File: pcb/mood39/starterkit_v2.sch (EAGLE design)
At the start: 7 parts, among them IC1 TINY85

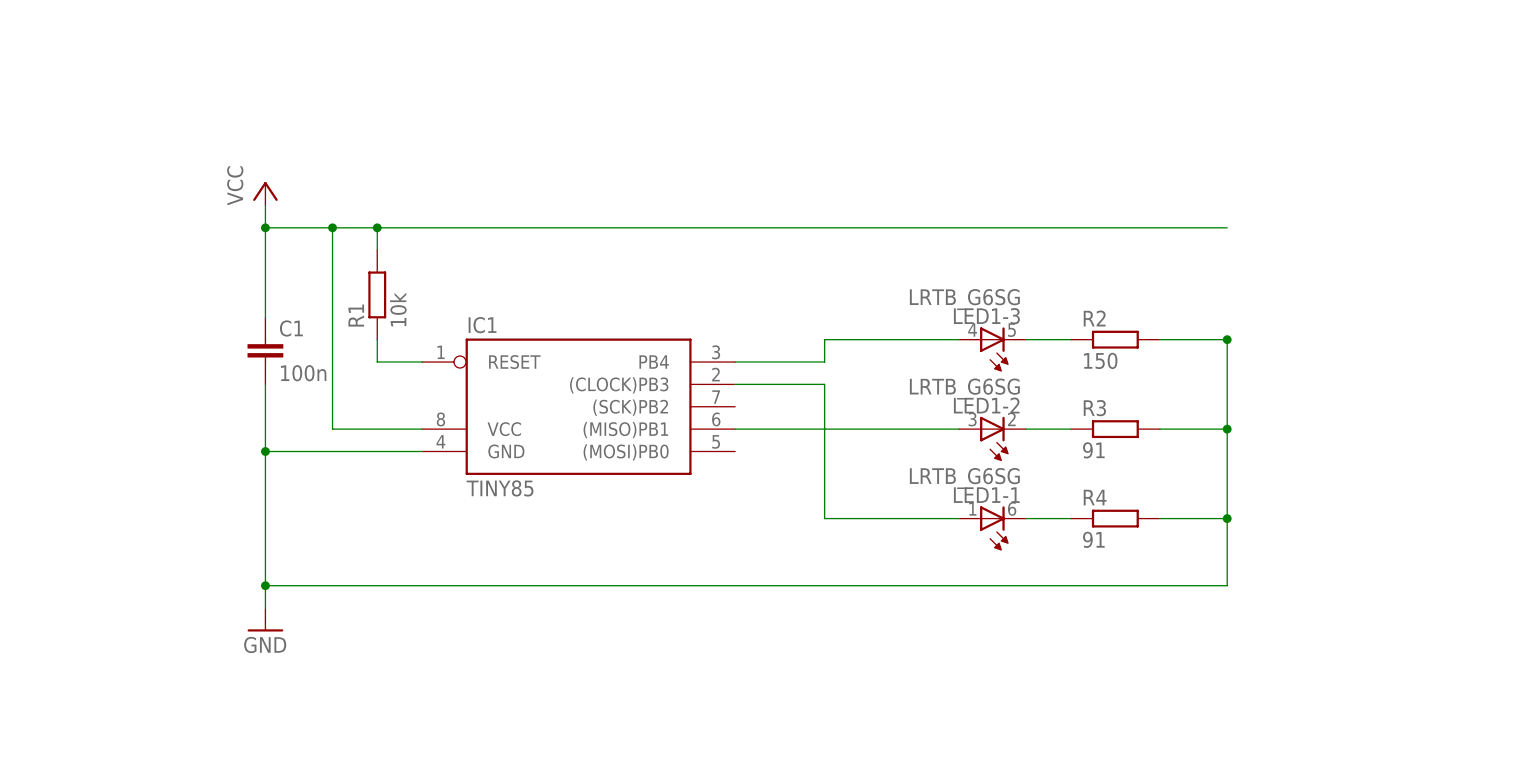
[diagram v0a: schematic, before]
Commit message: add some connectors and the voltage regulator
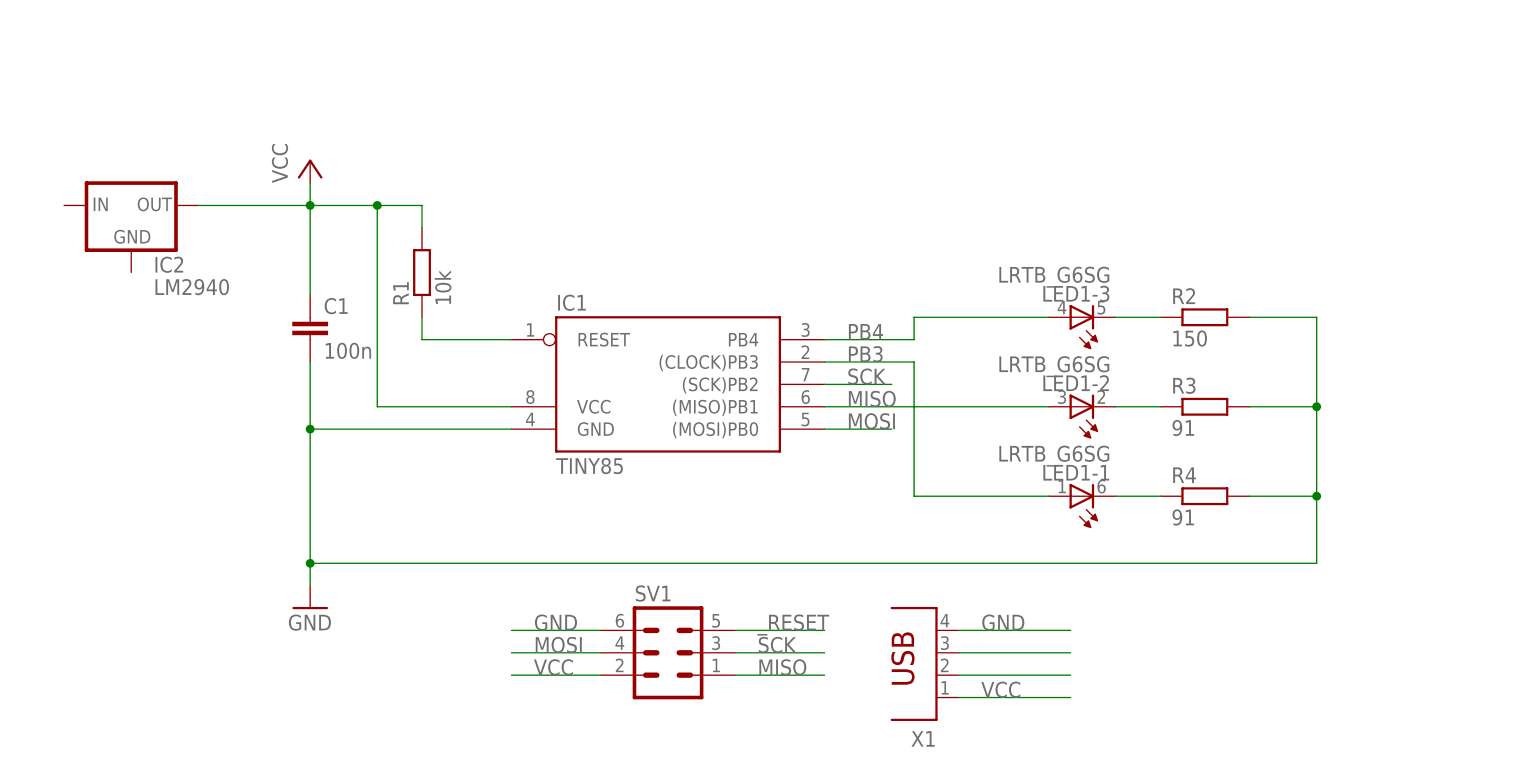
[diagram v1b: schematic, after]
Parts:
- added IC2: LM2940, v-reg:78XXL
- added SV1: (no value), con-ml:ML6
- added X1: (no value), con-berg:PN61729
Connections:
- net N$1 renamed PB4
- net N$3 renamed PB3
- removed net N$2: IC1.(MISO)PB1, LED1-2.A
- removed net N$4: IC1.RESET, R1.1
- new net MISO: IC1.(MISO)PB1, LED1-2.A, SV1.1
- new net MOSI: IC1.(MOSI)PB0, SV1.4
- new net SCK: IC1.(SCK)PB2, SV1.3
- new net USBD+: X1.3
- new net USBD-: X1.2
- new net _RESET: IC1.RESET, R1.1, SV1.5
- net GND: now also SV1.6, X1.4
- net VCC: now also IC2.OUT, SV1.2, X1.1
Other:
- moved on the sheet: C1, IC1, LED1-1, LED1-2, LED1-3, R1, R2, R3, R4

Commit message: add board (not routed) and design rules
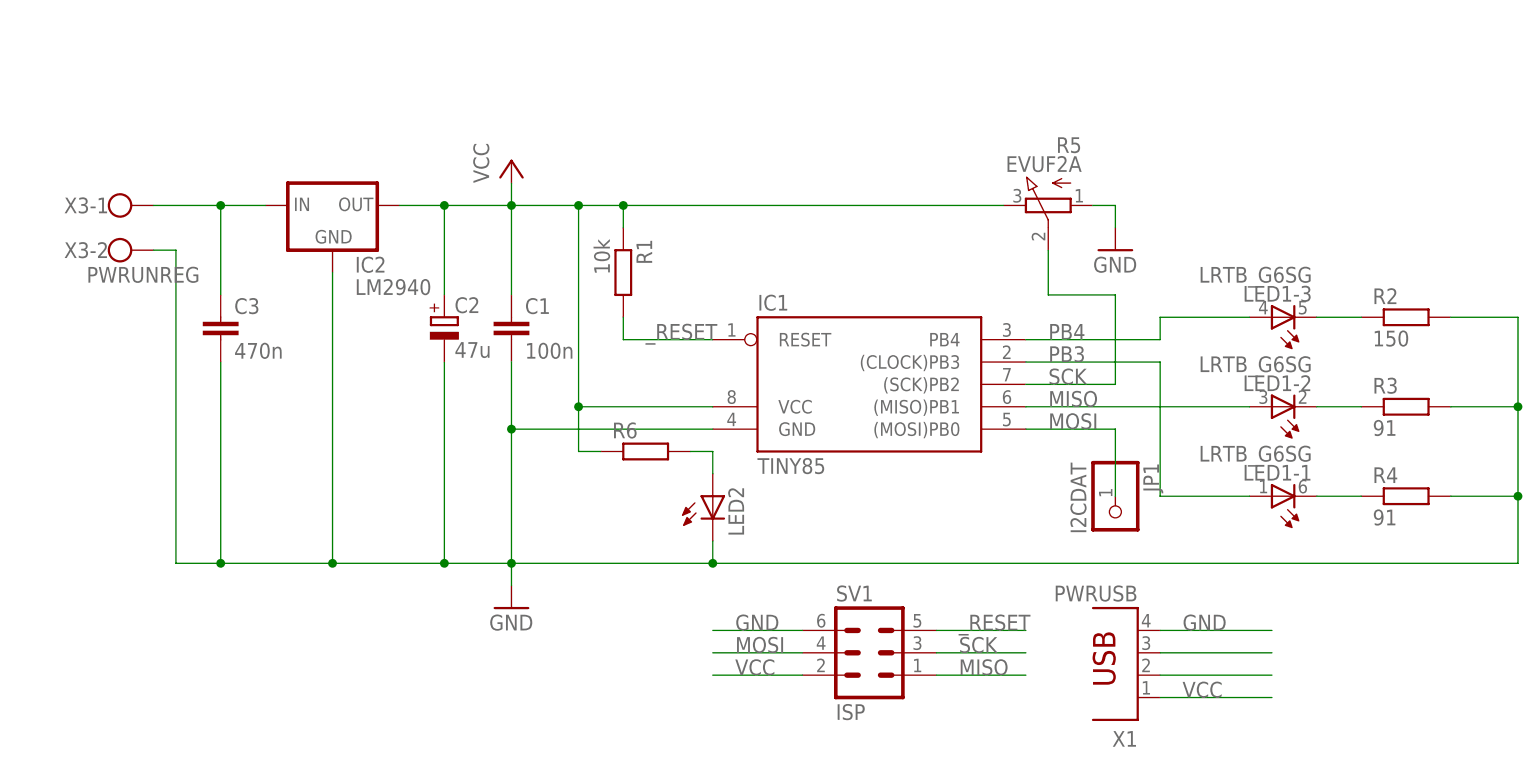
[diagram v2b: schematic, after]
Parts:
- added C2: 47u, rcl:CPOL-EUE2.5-5
- added C3: 470n, rcl:C-EU025-025X050
- added JP1: I2CDAT, pinhead:PINHD-1X1
- added LED2: (no value), led:LED3MM
- added R5: EVUF2A, pot:EVUF2A
- added R6: (no value), rcl:R-EU_R0805
- added X3: PWRUNREG, con-wago-500:W237-102
- C1: device rcl:C-EU025-025X050 -> rcl:C-EUC0805
- IC2: device v-reg:78XXL -> v-reg:78XXS
- R1, R2, R3, R4: device rcl:R-EU_0204/7 -> rcl:R-EU_R0805
- SV1: value (none) -> ISP
- X1: value (none) -> PWRUSB
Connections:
- new net N$1: LED2.A, R6.2
- new net N$2: C3.1, IC2.IN, X3-1.KL
- net GND: now also C2.-, C3.2, IC2.GND, LED2.C, R5.A, X3-2.KL
- net MOSI: now also JP1.1
- net SCK: now also R5.S
- net VCC: now also C2.+, R1.1, R5.E, R6.1; no longer R1.2
- net _RESET: now also R1.2; no longer R1.1
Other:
- moved on the sheet: C1, IC1, LED1-1, LED1-2, LED1-3, R1, R2, R3, R4, SV1, X1

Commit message: start routing
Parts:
- C3: device rcl:C-EU025-025X050 -> rcl:C-EUC0805
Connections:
- net N$2 renamed V+
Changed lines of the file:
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@@
 <clearance class="0" value="0.355"/>
+</class>
+<class number="1" name="supply" width="0.4064" drill="0">
 </class>
 </classes>
@@
 <part name="X3" library="con-wago-500" deviceset="W237-102" device="" value="PWRUNREG"/>
 <part name="C2" library="rcl" deviceset="CPOL-EU" device="E2.5-5" value="47u"/>
-<part name="C3" library="rcl" deviceset="C-EU" device="025-025X050" value="470n"/>
+<part name="C3" library="rcl" deviceset="C-EU" device="C0805" value="470n"/>
 <part name="R5" library="pot" deviceset="EVU" device="A" technology="F2"/>
 <part name="JP1" library="pinhead" deviceset="PINHD-1X1" device="" value="I2CDAT"/>
@@
 </segment>
 </net>
-<net name="GND" class="0">
+<net name="GND" class="1">
 <segment>
 <pinref part="C1" gate="G$1" pin="2"/>
@@
 </segment>
 </net>
-<net name="VCC" class="0">
+<net name="VCC" class="1">
 <segment>
 <pinref part="IC1" gate="G$1" pin="VCC"/>
@@
 </segment>
 </net>
-<net name="N$2" class="0">
+<net name="V+" class="1">
 <segment>
 <pinref part="X3" gate="-1" pin="KL"/>
@@
 <wire x1="-10.16" y1="68.58" x2="-10.16" y2="78.74" width="0.1524" layer="91"/>
 <junction x="-10.16" y="78.74"/>
-</segment>
-</net>
+<label x="-15.24" y="78.74" size="1.778" layer="95"/>
+</segment>
+</net>

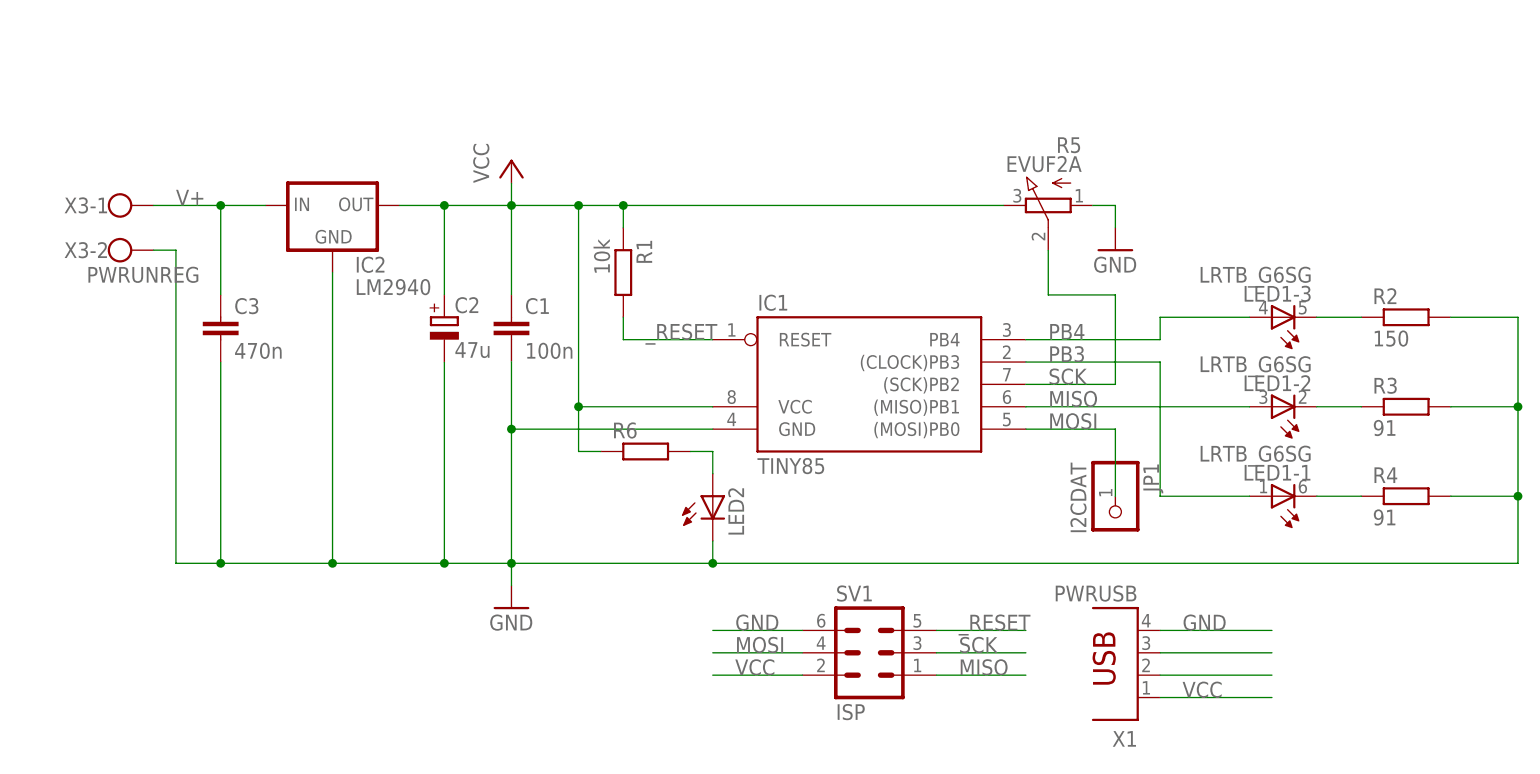
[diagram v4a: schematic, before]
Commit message: routing to a point where the right packages are needed
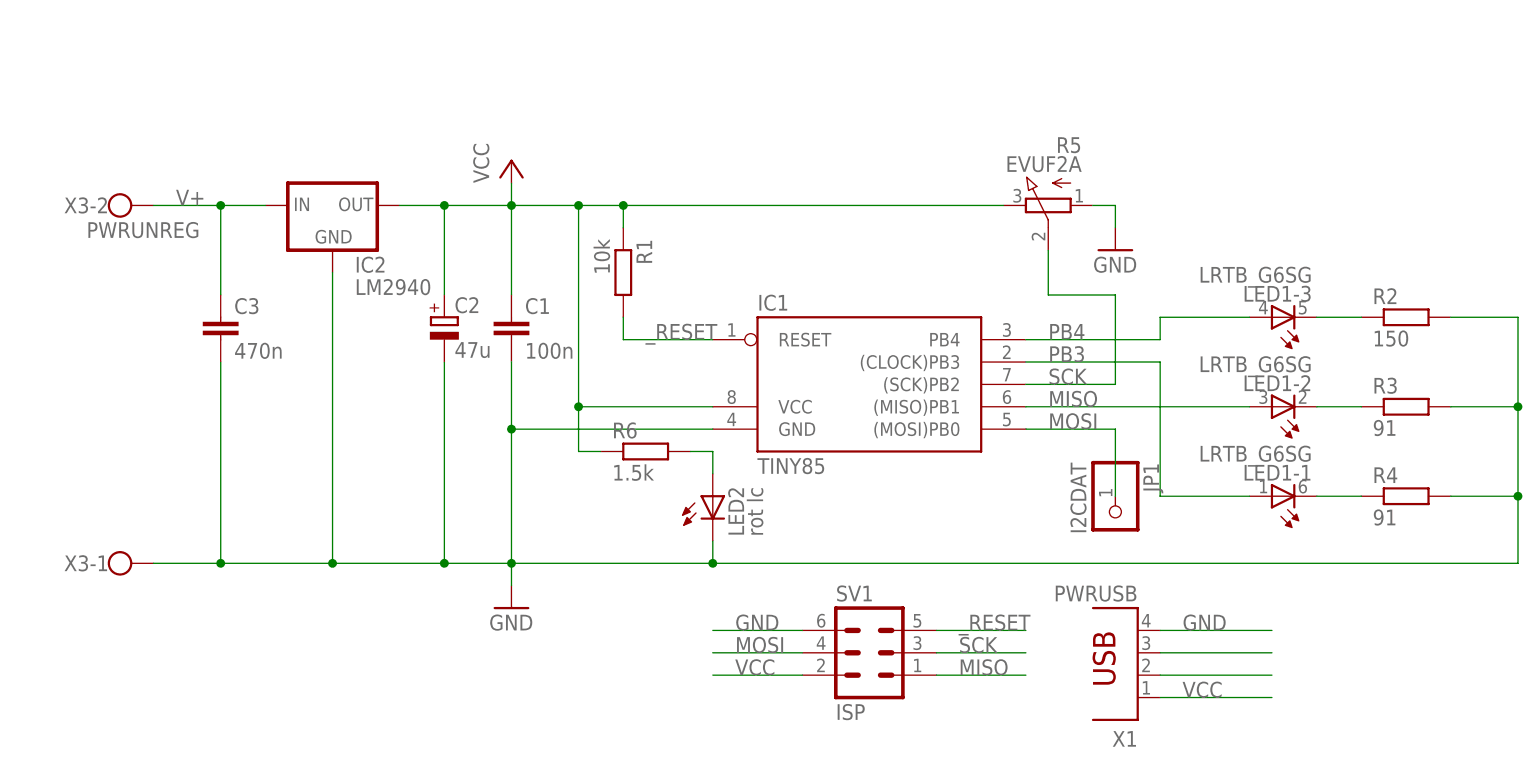
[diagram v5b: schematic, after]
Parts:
- LED2: value (none) -> rot lc
- R6: value (none) -> 1.5k
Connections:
- net GND: now also X3-1.KL; no longer X3-2.KL
- net V+: now also X3-2.KL; no longer X3-1.KL
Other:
- moved on the sheet: X3-1, X3-2
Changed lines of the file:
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@@
 <grid distance="0.1" unitdist="inch" unit="inch" style="lines" multiple="1" display="no" altdistance="0.01" altunitdist="inch" altunit="inch"/>
 <layers>
-<layer number="1" name="Top" color="4" fill="1" visible="yes" active="no"/>
-<layer number="16" name="Bottom" color="1" fill="1" visible="yes" active="no"/>
-<layer number="17" name="Pads" color="2" fill="1" visible="yes" active="no"/>
-<layer number="18" name="Vias" color="2" fill="1" visible="yes" active="no"/>
-<layer number="19" name="Unrouted" color="6" fill="1" visible="yes" active="no"/>
-<layer number="20" name="Dimension" color="15" fill="1" visible="yes" active="no"/>
-<layer number="21" name="tPlace" color="7" fill="1" visible="yes" active="no"/>
-<layer number="22" name="bPlace" color="7" fill="1" visible="yes" active="no"/>
-<layer number="23" name="tOrigins" color="15" fill="1" visible="yes" active="no"/>
-<layer number="24" name="bOrigins" color="15" fill="1" visible="yes" active="no"/>
-<layer number="25" name="tNames" color="7" fill="1" visible="yes" active="no"/>
-<layer number="26" name="bNames" color="7" fill="1" visible="yes" active="no"/>
-<layer number="27" name="tValues" color="7" fill="1" visible="yes" active="no"/>
-<layer number="28" name="bValues" color="7" fill="1" visible="yes" active="no"/>
+<layer number="1" name="Top" color="4" fill="1" visible="no" active="no"/>
+<layer number="16" name="Bottom" color="1" fill="1" visible="no" active="no"/>
+<layer number="17" name="Pads" color="2" fill="1" visible="no" active="no"/>
+<layer number="18" name="Vias" color="2" fill="1" visible="no" active="no"/>
+<layer number="19" name="Unrouted" color="6" fill="1" visible="no" active="no"/>
+<layer number="20" name="Dimension" color="15" fill="1" visible="no" active="no"/>
+<layer number="21" name="tPlace" color="7" fill="1" visible="no" active="no"/>
+<layer number="22" name="bPlace" color="7" fill="1" visible="no" active="no"/>
+<layer number="23" name="tOrigins" color="15" fill="1" visible="no" active="no"/>
+<layer number="24" name="bOrigins" color="15" fill="1" visible="no" active="no"/>
+<layer number="25" name="tNames" color="7" fill="1" visible="no" active="no"/>
+<layer number="26" name="bNames" color="7" fill="1" visible="no" active="no"/>
+<layer number="27" name="tValues" color="7" fill="1" visible="no" active="no"/>
+<layer number="28" name="bValues" color="7" fill="1" visible="no" active="no"/>
 <layer number="29" name="tStop" color="7" fill="3" visible="no" active="no"/>
 <layer number="30" name="bStop" color="7" fill="6" visible="no" active="no"/>
@@
 <layer number="35" name="tGlue" color="7" fill="4" visible="no" active="no"/>
 <layer number="36" name="bGlue" color="7" fill="5" visible="no" active="no"/>
-<layer number="37" name="tTest" color="7" fill="1" visible="yes" active="no"/>
-<layer number="38" name="bTest" color="7" fill="1" visible="yes" active="no"/>
+<layer number="37" name="tTest" color="7" fill="1" visible="no" active="no"/>
+<layer number="38" name="bTest" color="7" fill="1" visible="no" active="no"/>
 <layer number="39" name="tKeepout" color="4" fill="11" visible="no" active="no"/>
 <layer number="40" name="bKeepout" color="1" fill="11" visible="no" active="no"/>
@@
 <layer number="44" name="Drills" color="7" fill="1" visible="no" active="no"/>
 <layer number="45" name="Holes" color="7" fill="1" visible="no" active="no"/>
-<layer number="46" name="Milling" color="3" fill="1" visible="yes" active="no"/>
-<layer number="47" name="Measures" color="7" fill="1" visible="yes" active="no"/>
-<layer number="48" name="Document" color="7" fill="1" visible="yes" active="no"/>
-<layer number="49" name="Reference" color="7" fill="1" visible="yes" active="no"/>
-<layer number="51" name="tDocu" color="7" fill="1" visible="yes" active="no"/>
-<layer number="52" name="bDocu" color="7" fill="1" visible="yes" active="no"/>
+<layer number="46" name="Milling" color="3" fill="1" visible="no" active="no"/>
+<layer number="47" name="Measures" color="7" fill="1" visible="no" active="no"/>
+<layer number="48" name="Document" color="7" fill="1" visible="no" active="no"/>
+<layer number="49" name="Reference" color="7" fill="1" visible="no" active="no"/>
+<layer number="51" name="tDocu" color="7" fill="1" visible="no" active="no"/>
+<layer number="52" name="bDocu" color="7" fill="1" visible="no" active="no"/>
 <layer number="91" name="Nets" color="2" fill="1" visible="yes" active="yes"/>
 <layer number="92" name="Busses" color="1" fill="1" visible="yes" active="yes"/>
@@
 <part name="JP1" library="pinhead" deviceset="PINHD-1X1" device="" value="I2CDAT"/>
 <part name="GND2" library="supply1" deviceset="GND" device=""/>
-<part name="LED2" library="led" deviceset="LED" device="3MM"/>
-<part name="R6" library="rcl" deviceset="R-EU_" device="R0805"/>
+<part name="LED2" library="led" deviceset="LED" device="3MM" value="rot lc"/>
+<part name="R6" library="rcl" deviceset="R-EU_" device="R0805" value="1.5k"/>
 </parts>
 <sheets>
@@
 <instance part="X1" gate="G$1" x="93.98" y="27.94" rot="R180"/>
 <instance part="IC2" gate="1" x="2.54" y="78.74"/>
-<instance part="X3" gate="-1" x="-22.86" y="78.74"/>
-<instance part="X3" gate="-2" x="-22.86" y="73.66"/>
+<instance part="X3" gate="-1" x="-22.86" y="38.1"/>
+<instance part="X3" gate="-2" x="-22.86" y="78.74"/>
 <instance part="C2" gate="G$1" x="15.24" y="66.04"/>
 <instance part="C3" gate="G$1" x="-10.16" y="66.04"/>
@@
 <junction x="137.16" y="45.72"/>
 <junction x="137.16" y="55.88"/>
-<pinref part="X3" gate="-2" pin="KL"/>
-<wire x1="-17.78" y1="73.66" x2="-15.24" y2="73.66" width="0.1524" layer="91"/>
-<wire x1="-15.24" y1="73.66" x2="-15.24" y2="38.1" width="0.1524" layer="91"/>
-<wire x1="-15.24" y1="38.1" x2="-10.16" y2="38.1" width="0.1524" layer="91"/>
+<wire x1="-17.78" y1="38.1" x2="-10.16" y2="38.1" width="0.1524" layer="91"/>
 <pinref part="IC2" gate="1" pin="GND"/>
 <wire x1="-10.16" y1="38.1" x2="2.54" y2="38.1" width="0.1524" layer="91"/>
@@
 <wire x1="45.72" y1="40.64" x2="45.72" y2="38.1" width="0.1524" layer="91"/>
 <junction x="45.72" y="38.1"/>
+<pinref part="X3" gate="-1" pin="KL"/>
 </segment>
 <segment>
@@
 <net name="V+" class="1">
 <segment>
-<pinref part="X3" gate="-1" pin="KL"/>
 <pinref part="IC2" gate="1" pin="IN"/>
-<wire x1="-17.78" y1="78.74" x2="-10.16" y2="78.74" width="0.1524" layer="91"/>
 <pinref part="C3" gate="G$1" pin="1"/>
 <wire x1="-10.16" y1="78.74" x2="-5.08" y2="78.74" width="0.1524" layer="91"/>
 <wire x1="-10.16" y1="68.58" x2="-10.16" y2="78.74" width="0.1524" layer="91"/>
+<label x="-15.24" y="78.74" size="1.778" layer="95"/>
+<pinref part="X3" gate="-2" pin="KL"/>
+<wire x1="-17.78" y1="78.74" x2="-10.16" y2="78.74" width="0.1524" layer="91"/>
 <junction x="-10.16" y="78.74"/>
-<label x="-15.24" y="78.74" size="1.778" layer="95"/>
-</segment>
-</net>
+</segment>
+</net>

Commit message: der miniaturtaster ist arg groß
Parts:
- added S1: (no value), switch-omron:10-XX
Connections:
- net GND: now also S1.P, S1.P1
- net MOSI: now also S1.S, S1.S1
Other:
- moved on the sheet: C1, C2, C3, IC1, IC2, JP1, LED2, R1, R5, R6, X3-1, X3-2
